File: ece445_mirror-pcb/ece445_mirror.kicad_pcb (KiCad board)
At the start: 2 copper layers, 50 x 51 mm, 49 parts, among them J1 Conn_ARM_JTAG_SWD_10, J2 LED_CONN, J3 Conn_01x06, J4 USB_C_Receptacle_USB2.0_14P, J5 Conn_01x04, J6 button, J7 boot_switch, J8 Photoresistor, J9 LED_STRIP, U2 STM32F401RBTx, U3 USBLC6-2SC6, U4 AP2112K-3.3, Y1 25MHz

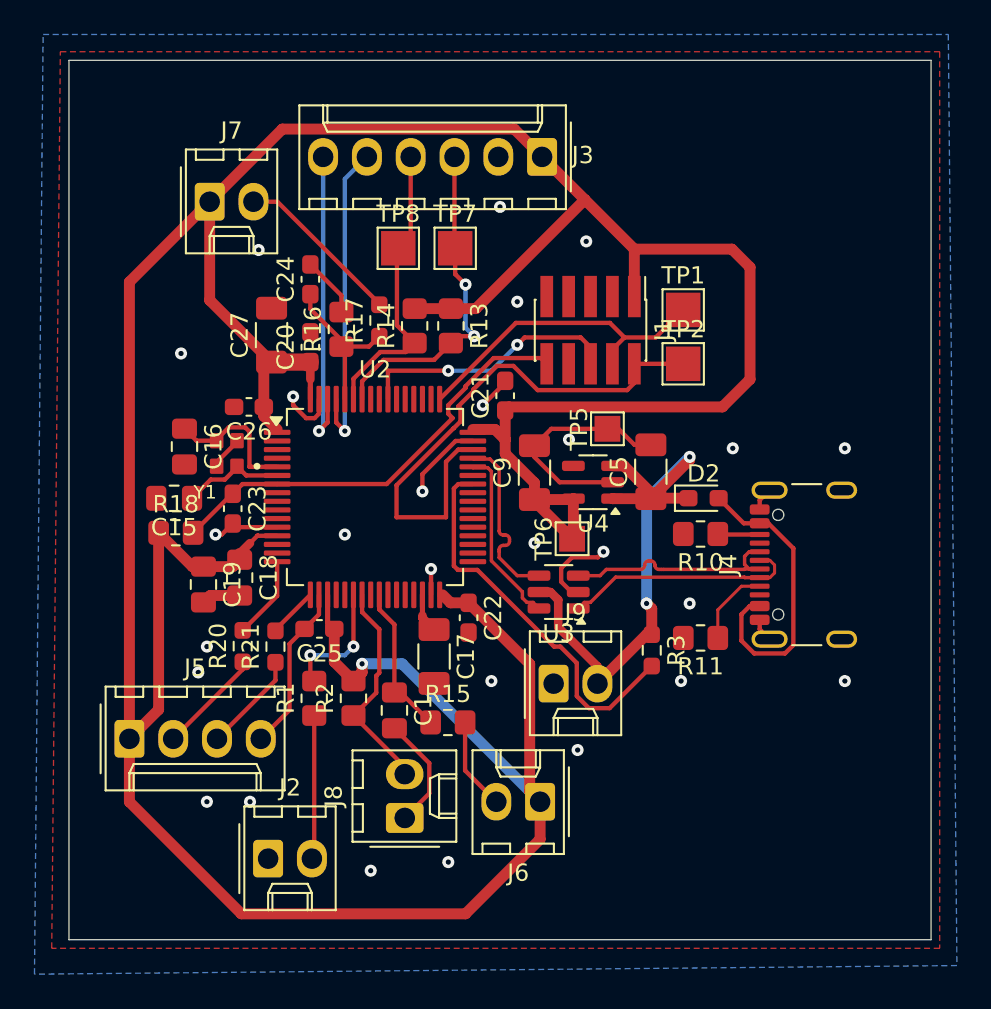
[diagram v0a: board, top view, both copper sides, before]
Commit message: fixed silkscreen
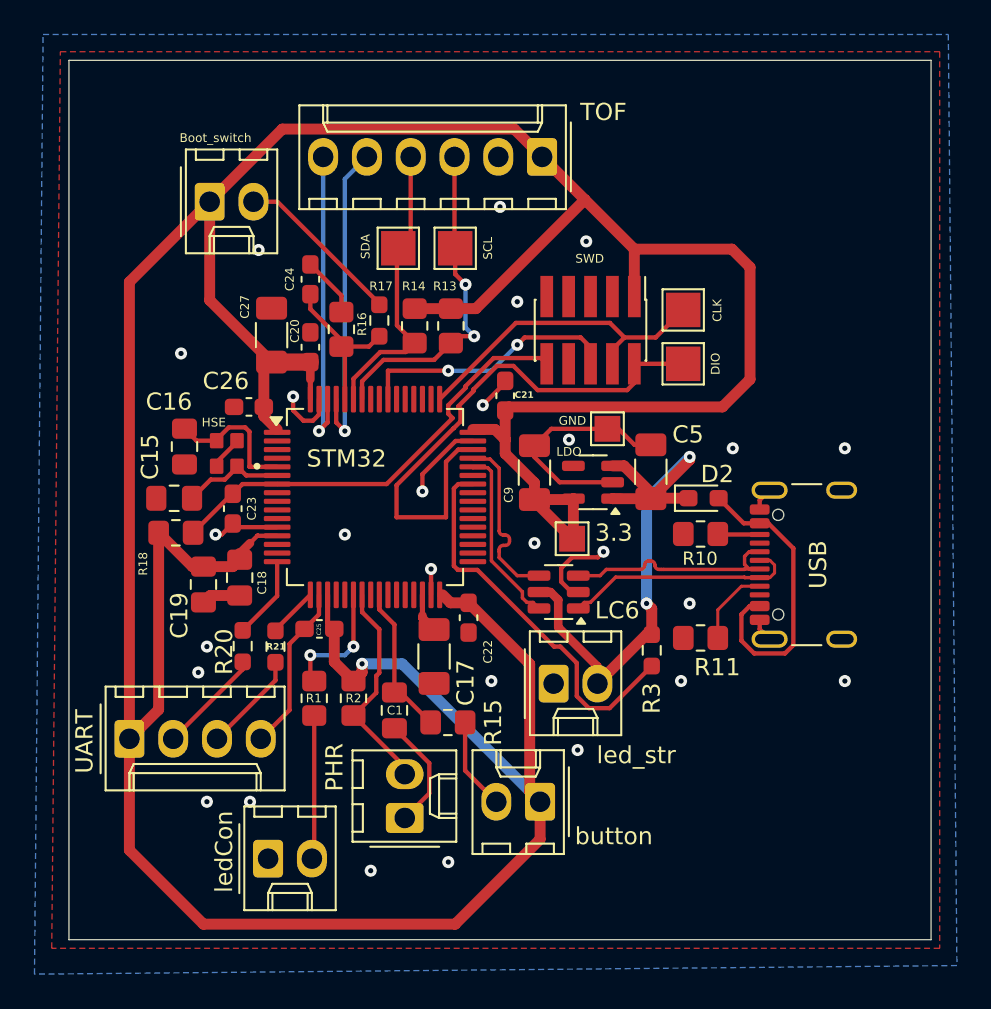
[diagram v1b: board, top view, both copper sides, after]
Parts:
- renumbered TP6 to 3.3, J7 to Boot_switch, TP1 to CLK, TP2 to DIO, TP5 to GND, Y1 to HSE, U3 to LC6, U4 to LDO, J8 to PHR, TP7 to SCL, TP8 to SDA, U2 to STM32, J1 to SWD, J3 to TOF, J5 to UART, J4 to USB, J6 to button, J2 to ledCon, J9 to led_str
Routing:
- net +3.3V: track 232.4 -> 234.6 mm
